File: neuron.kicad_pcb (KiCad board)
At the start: 2 copper layers, 98.5 x 59.8 mm, 90 parts, among them J1 Conn_02x01, J2 Conn_02x01, J3 Conn_02x01, J4 Conn_02x03, Q1 2sk3018, Q10 2sk3018, Q11 2sk3018, Q12 2sk3018, Q2 2sk3018, Q3 2sk3018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

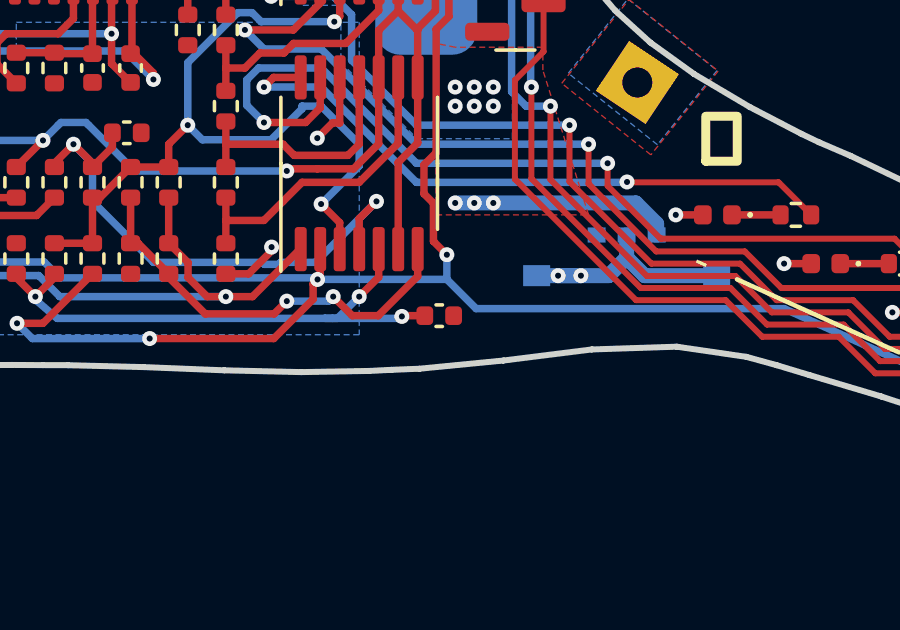
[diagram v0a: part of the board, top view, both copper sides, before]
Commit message: Add hysteresis for refractory time comparator
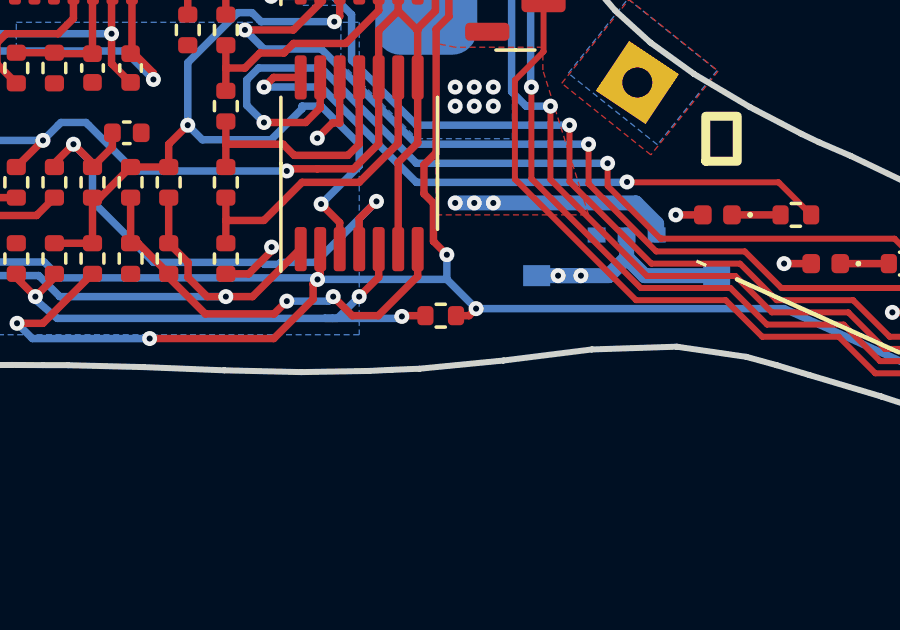
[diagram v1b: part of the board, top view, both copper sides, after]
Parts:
- removed C8: 100n, Capacitor_SMD:C_0402_1005Metric
- added R45: 100k, Resistor_SMD:R_0402_1005Metric, F.Cu at (98.6, 77.5)
- R22: value 22k -> 27k
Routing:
- net /RESET: track 99.3 -> 100.0 mm, vias 5 -> 6
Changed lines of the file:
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@@
 			)
 		)
-		(property "Value" "22k"
+		(property "Value" "27k"
 			(at 0 1.17 90)
 			(layer "F.Fab")
@@
 			)
 		)
-		(property "LCSC" "C25768"
+		(property "LCSC" "C25771"
 			(at 10.16 161.29 0)
 			(layer "F.Fab")
@@
 		)
 	)
+	(footprint "Resistor_SMD:R_0402_1005Metric"
+		(layer "F.Cu")
+		(at 98.6024 77.47 180)
+		(descr "Resistor SMD 0402 (1005 Metric), square (rectangular) end terminal, IPC-7351 nominal, (Body size source: IPC-SM-782 page 72, https://www.pcb-3d.com/wordpress/wp-content/uploads/ipc-sm-782a_amendment_1_and_2.pdf), generated with kicad-footprint-generator")
+		(tags "resistor")
+		(property "Reference" "R45"
+			(at 0 -1.17 0)
+			(layer "F.SilkS")
+			(hide yes)
+			(effects
+				(font
+					(size 1 1)
+					(thickness 0.15)
+				)
+			)
+		)
+		(property "Value" "100k"
+			(at 0 1.17 0)
+			(layer "F.Fab")
+			(effects
+				(font
+					(size 1 1)
+					(thickness 0.15)
+				)
+			)
+		)
+		(property "Datasheet" ""
+			(at 0 0 0)
+			(layer "F.Fab")
+			(hide yes)
+			(effects
+				(font
+					(size 1.27 1.27)
+					(thickness 0.15)
+				)
+			)
+		)
+		(property "Description" ""
+			(at 0 0 0)
+			(layer "F.Fab")
+			(hide yes)
+			(effects
+				(font
+					(size 1.27 1.27)
+					(thickness 0.15)
+				)
+			)
+		)
+		(property "LCSC" "C25741"
+			(at 0 0 180)
+			(unlocked yes)
+			(layer "F.Fab")
+			(hide yes)
+			(effects
+				(font
+					(size 1 1)
+					(thickness 0.15)
+				)
+			)
+		)
+		(property ki_fp_filters "R_*")
+		(sheetname "/")
+		(sheetfile "neuron.kicad_sch")
+		(attr smd)
+		(fp_line
+			(start -0.153641 0.38)
+			(end 0.153641 0.38)
+			(stroke
+				(width 0.12)
+				(type solid)
+			)
+			(layer "F.SilkS")
+		)
+		(fp_line
+			(start -0.153641 -0.38)
+			(end 0.153641 -0.38)
+			(stroke
+				(width 0.12)
+				(type solid)
+			)
+			(layer "F.SilkS")
+		)
+		(fp_line
+			(start 0.93 0.47)
+			(end -0.93 0.47)
+			(stroke
+				(width 0.05)
+				(type solid)
+			)
+			(layer "F.CrtYd")
+		)
+		(fp_line
+			(start 0.93 -0.47)
+			(end 0.93 0.47)
+			(stroke
+				(width 0.05)
+				(type solid)
+			)
+			(layer "F.CrtYd")
+		)
+		(fp_line
+			(start -0.93 0.47)
+			(end -0.93 -0.47)
+			(stroke
+				(width 0.05)
+				(type solid)
+			)
+			(layer "F.CrtYd")
+		)
+		(fp_line
+			(start -0.93 -0.47)
+			(end 0.93 -0.47)
+			(stroke
+				(width 0.05)
+				(type solid)
+			)
+			(layer "F.CrtYd")
+		)
+		(fp_line
+			(start 0.525 0.27)
+			(end -0.525 0.27)
+			(stroke
+				(width 0.1)
+				(type solid)
+			)
+			(layer "F.Fab")
+		)
+		(fp_line
+			(start 0.525 -0.27)
+			(end 0.525 0.27)
+			(stroke
+				(width 0.1)
+				(type solid)
+			)
+			(layer "F.Fab")
+		)
+		(fp_line
+			(start -0.525 0.27)
+			(end -0.525 -0.27)
+			(stroke
+				(width 0.1)
+				(type solid)
+			)
+			(layer "F.Fab")
+		)
+		(fp_line
+			(start -0.525 -0.27)
+			(end 0.525 -0.27)
+			(stroke
+				(width 0.1)
+				(type solid)
+			)
+			(layer "F.Fab")
+		)
+		(fp_text user "${REFERENCE}"
+			(at 0 0 0)
+			(layer "F.Fab")
+			(effects
+				(font
+					(size 0.26 0.26)
+					(thickness 0.04)
+				)
+			)
+		)
+		(pad "1" smd roundrect
+			(at -0.51 0 180)
+			(size 0.54 0.64)
+			(layers "F.Cu" "F.Mask" "F.Paste")
+			(roundrect_rratio 0.25)
+			(net 12 "/RESET")
+			(pintype "passive")
+		)
+		(pad "2" smd roundrect
+			(at 0.51 0 180)
+			(size 0.54 0.64)
+			(layers "F.Cu" "F.Mask" "F.Paste")
+			(roundrect_rratio 0.25)
+			(net 43 "Net-(U3A-+)")
+			(pintype "passive")
+		)
+		(embedded_fonts no)
+		(model "${KICAD9_3DMODEL_DIR}/Resistor_SMD.3dshapes/R_0402_1005Metric.wrl"
+			(offset
+				(xyz 0 0 0)
+			)
+			(scale
+				(xyz 1 1 1)
+			)
+			(rotate
+				(xyz 0 0 0)
+			)
+		)
+	)
 	(footprint "Custom:Testpad"
 		(layer "F.Cu")
@@
 		)
 	)
-	(footprint "Capacitor_SMD:C_0402_1005Metric"
-		(layer "F.Cu")
-		(at 98.552 77.47 180)
-		(descr "Capacitor SMD 0402 (1005 Metric), square (rectangular) end terminal, IPC_7351 nominal, (Body size source: IPC-SM-782 page 76, https://www.pcb-3d.com/wordpress/wp-content/uploads/ipc-sm-782a_amendment_1_and_2.pdf), generated with kicad-footprint-generator")
-		(tags "capacitor")
-		(property "Reference" "C8"
-			(at 0 -1.16 0)
-			(layer "User.1")
-			(effects
-				(font
-					(size 1 1)
-					(thickness 0.15)
-				)
-			)
-		)
-		(property "Value" "100n"
-			(at 0 1.16 0)
-			(layer "F.Fab")
-			(effects
-				(font
-					(size 1 1)
-					(thickness 0.15)
-				)
-			)
-		)
-		(property "Datasheet" ""
-			(at 0 0 180)
-			(layer "F.Fab")
-			(hide yes)
-			(effects
-				(font
-					(size 1.27 1.27)
-					(thickness 0.15)
-				)
-			)
-		)
-		(property "Description" ""
-			(at 0 0 180)
-			(layer "F.Fab")
-			(hide yes)
-			(effects
-				(font
-					(size 1.27 1.27)
-					(thickness 0.15)
-				)
-			)
-		)
-		(property "LCSC" "C1525"
-			(at 197.104 154.94 0)
-			(layer "F.Fab")
-			(hide yes)
-			(effects
-				(font
-					(size 1 1)
-					(thickness 0.15)
-				)
-			)
-		)
-		(property ki_fp_filters "C_*")
-		(sheetname "/")
-		(sheetfile "neuron.kicad_sch")
-		(attr smd)
-		(fp_line
-			(start -0.107836 0.36)
-			(end 0.107836 0.36)
-			(stroke
-				(width 0.12)
-				(type solid)
-			)
-			(layer "F.SilkS")
-		)
-		(fp_line
-			(start -0.107836 -0.36)
-			(end 0.107836 -0.36)
-			(stroke
-				(width 0.12)
-				(type solid)
-			)
-			(layer "F.SilkS")
-		)
-		(fp_line
-			(start 0.91 0.46)
-			(end -0.91 0.46)
-			(stroke
-				(width 0.05)
-				(type solid)
-			)
-			(layer "F.CrtYd")
-		)
-		(fp_line
-			(start 0.91 -0.46)
-			(end 0.91 0.46)
-			(stroke
-				(width 0.05)
-				(type solid)
-			)
-			(layer "F.CrtYd")
-		)
-		(fp_line
-			(start -0.91 0.46)
-			(end -0.91 -0.46)
-			(stroke
-				(width 0.05)
-				(type solid)
-			)
-			(layer "F.CrtYd")
-		)
-		(fp_line
-			(start -0.91 -0.46)
-			(end 0.91 -0.46)
-			(stroke
-				(width 0.05)
-				(type solid)
-			)
-			(layer "F.CrtYd")
-		)
-		(fp_line
-			(start 0.5 0.25)
-			(end -0.5 0.25)
-			(stroke
-				(width 0.1)
-				(type solid)
-			)
-			(layer "F.Fab")
-		)
-		(fp_line
-			(start 0.5 -0.25)
-			(end 0.5 0.25)
-			(stroke
-				(width 0.1)
-				(type solid)
-			)
-			(layer "F.Fab")
-		)
-		(fp_line
-			(start -0.5 0.25)
-			(end -0.5 -0.25)
-			(stroke
-				(width 0.1)
-				(type solid)
-			)
-			(layer "F.Fab")
-		)
-		(fp_line
-			(start -0.5 -0.25)
-			(end 0.5 -0.25)
-			(stroke
-				(width 0.1)
-				(type solid)
-			)
-			(layer "F.Fab")
-		)
-		(fp_text user "${REFERENCE}"
-			(at 0 0 0)
-			(layer "F.Fab")
-			(effects
-				(font
-					(size 0.25 0.25)
-					(thickness 0.04)
-				)
-			)
-		)
-		(pad "1" smd roundrect
-			(at -0.48 0 180)
-			(size 0.56 0.62)
-			(layers "F.Cu" "F.Mask" "F.Paste")
-			(roundrect_rratio 0.25)
-			(net 2 "GND")
-			(pintype "passive")
-		)
-		(pad "2" smd roundrect
-			(at 0.48 0 180)
-			(size 0.56 0.62)
-			(layers "F.Cu" "F.Mask" "F.Paste")
-			(roundrect_rratio 0.25)
-			(net 43 "Net-(U3A-+)")
-			(pintype "passive")
-		)
-		(embedded_fonts no)
-		(model "${KICAD6_3DMODEL_DIR}/Capacitor_SMD.3dshapes/C_0402_1005Metric.wrl"
-			(offset
-				(xyz 0 0 0)
-			)
-			(scale
-				(xyz 1 1 1)
-			)
-			(rotate
-				(xyz 0 0 0)
-			)
-		)
-	)
 	(footprint "Custom:Potentiometer"
 		(layer "F.Cu")
@@
 	)
 	(segment
+		(start 99.546 77.47)
+		(end 99.781 77.235)
+		(width 0.25)
+		(layer "F.Cu")
+		(net 12)
+	)
+	(segment
 		(start 98.36 74.992)
 		(end 98.806 75.438)
@@
 	)
 	(segment
+		(start 99.1124 77.47)
+		(end 99.546 77.47)
+		(width 0.25)
+		(layer "F.Cu")
+		(net 12)
+	)
+	(segment
 		(start 84.48 77.724)
 		(end 85.344 77.724)
@@
 		(size 0.5)
 		(drill 0.2)
+		(layers "F.Cu" "B.Cu")
+		(net 12)
+	)
+	(via
+		(at 99.781 77.235)
+		(size 0.5)
+		(drill 0.2)

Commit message: Update layout
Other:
- board text added: "Lu.i 03/2025 - giantaxon.org"
- board text added: "from Heidelberg & Bern made with by YS, SB & JG"
- board text removed: "Lu.i 09/2023 - giantaxon.org made with by YS, SB & JG"
- board text removed: "Uni HD, co-funded by the EU"
- board text removed: "n.brainscales.eu"
